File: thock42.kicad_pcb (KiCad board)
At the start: 2 copper layers, 132 x 100.7 mm, 78 parts, among them J1 OLED-128x32, SW1 SW_Push, SW10 SW_Push, SW11 SW_Push, SW12 SW_Push, SW13 SW_Push, SW14 SW_Push, SW15 SW_Push, SW16 SW_Push, SW17 SW_Push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

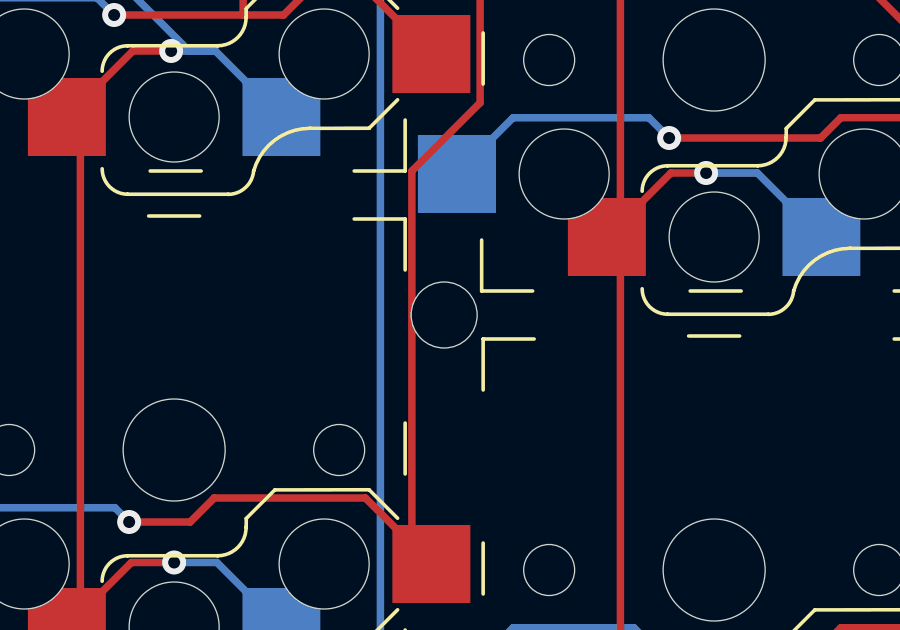
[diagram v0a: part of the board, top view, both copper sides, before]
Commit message: move mounting point
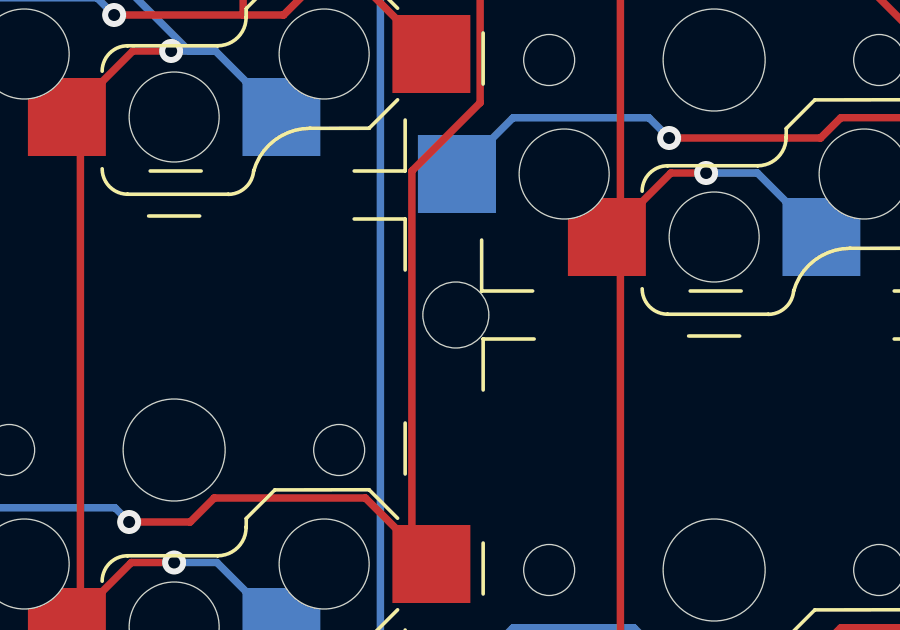
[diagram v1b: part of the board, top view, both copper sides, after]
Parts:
- moved REF** 0.39 mm to (159.9, 81.5)
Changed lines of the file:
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@@
 		(fp_arc
 			(start -2.448959 -7.624479)
-			(mid -2.2 -8.225519)
+			(mid -2.2 -8.22552)
 			(end -1.598959 -8.474481)
 			(stroke
@@
 		(fp_arc
 			(start -2.65 -7.700001)
-			(mid -3.350397 -6.672891)
+			(mid -3.350397 -6.67289)
 			(end -4.528858 -6.276988)
 			(stroke
@@
 		(fp_arc
 			(start -6.9 -5.9)
-			(mid -6.607107 -6.607107)
+			(mid -6.607107 -6.607108)
 			(end -5.9 -6.9)
 			(stroke
@@
 		(fp_arc
 			(start -5.9 6.9)
-			(mid -6.607107 6.607107)
+			(mid -6.607108 6.607107)
 			(end -6.9 5.9)
 			(stroke
@@
 	(footprint "MountingHole:MountingHole_2.2mm_M2"
 		(layer "F.Cu")
-		(at 159.5 81.5)
+		(at 159.89 81.5)
 		(descr "Mounting Hole 2.2mm, no annular, M2")
 		(tags "mounting hole 2.2mm no annular m2")
@@
 		)
 		(fp_line
-			(start -6.000001 7.699998)
+			(start -6.000001 7.699997)
 			(end -7.700002 7.7)
 			(stroke
@@
 		(fp_arc
 			(start -2.65 -7.7)
-			(mid -3.350399 -6.672893)
+			(mid -3.350399 -6.672894)
 			(end -4.528858 -6.276988)
 			(stroke
@@
 		(fp_line
 			(start 8 8.5)
-			(end -8.000002 8.5)
+			(end -8.000003 8.5)
 			(stroke
 				(width 0.15)
@@
 		(fp_line
 			(start -8 -8.5)
-			(end 8.000002 -8.5)
+			(end 8.000003 -8.5)
 			(stroke
 				(width 0.15)
@@
 		)
 		(fp_arc
-			(start 8.000002 -8.5)
-			(mid 8.707107 -8.207106)
+			(start 8.000003 -8.5)
+			(mid 8.707108 -8.207106)
 			(end 9 -7.5)
 			(stroke
@@
 		)
 		(fp_arc
-			(start -8.000002 8.5)
+			(start -8.000003 8.5)
 			(mid -8.707107 8.207107)
 			(end -9 7.5)

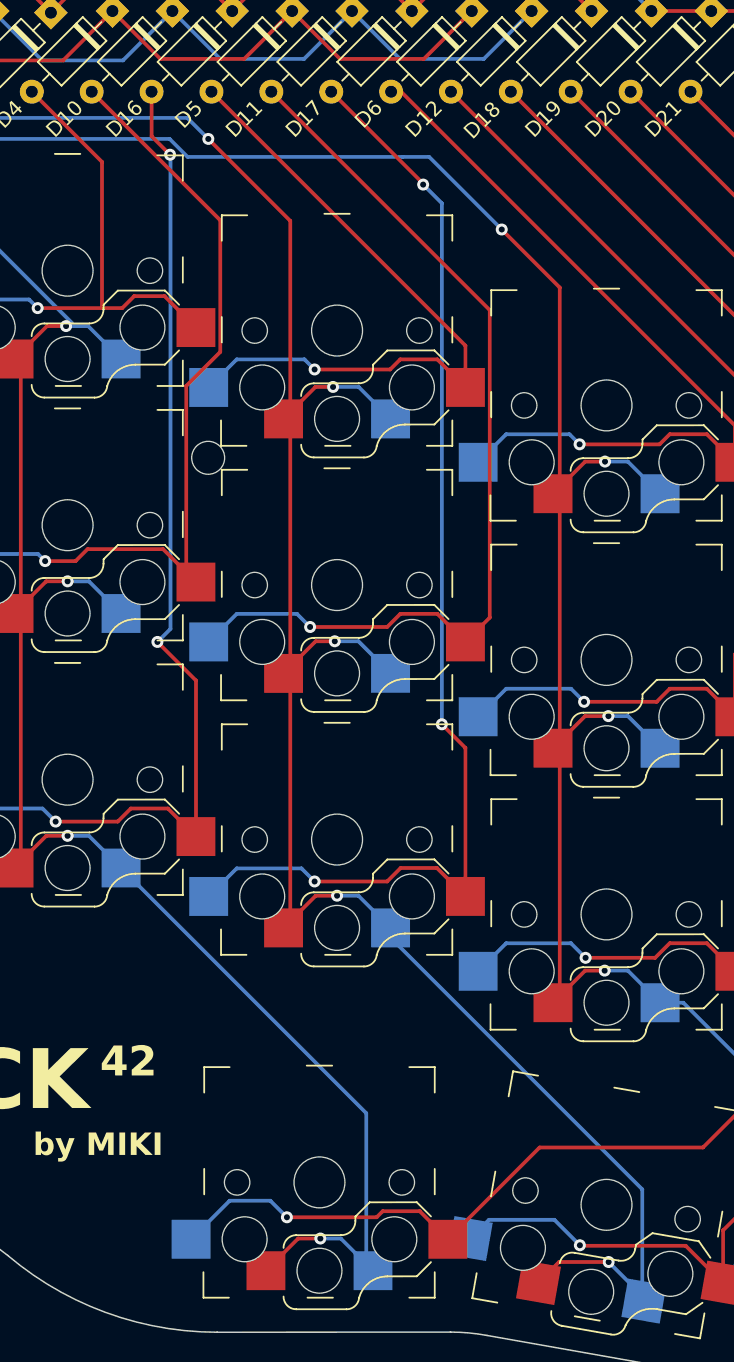
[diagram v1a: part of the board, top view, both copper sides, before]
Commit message: move index col down to align with ring col
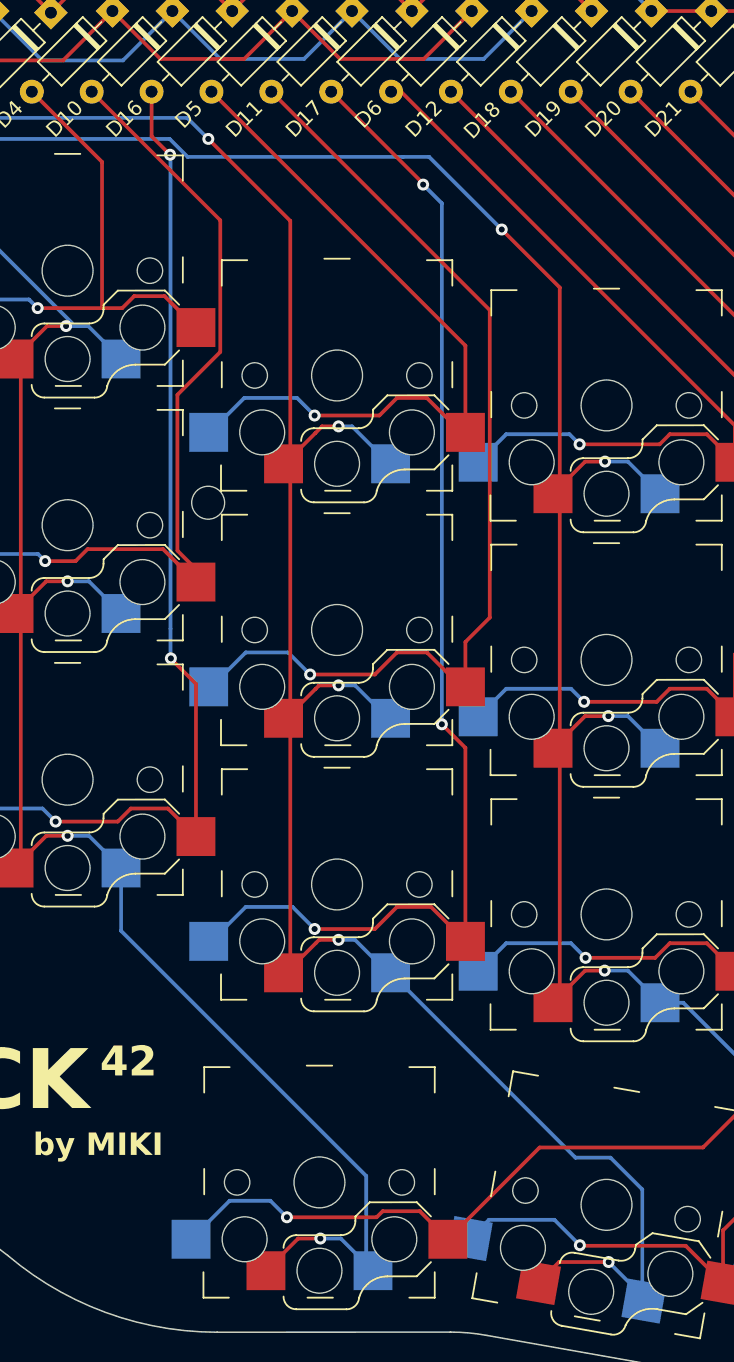
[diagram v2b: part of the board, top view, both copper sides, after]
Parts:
- moved REF** 3.00 mm to (159.9, 84.5)
- moved SW11 3.00 mm to (168.5, 93.0)
- moved SW17 3.00 mm to (168.5, 110.0)
- moved SW5 3.00 mm to (168.5, 76.0)
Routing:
- net Net-(D11-A): track 62.9 -> 66.8 mm
- net Net-(D17-A): track 76.9 -> 80.8 mm
- net Net-(D5-A): track 46.0 -> 49.8 mm
- net COL4: track 181.2 -> 184.0 mm
- net Net-(D10-A): track 56.9 -> 59.1 mm
- net Net-(D16-A): track 71.1 -> 70.4 mm
